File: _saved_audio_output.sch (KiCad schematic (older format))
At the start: 21 parts, among them U8 OPA1664

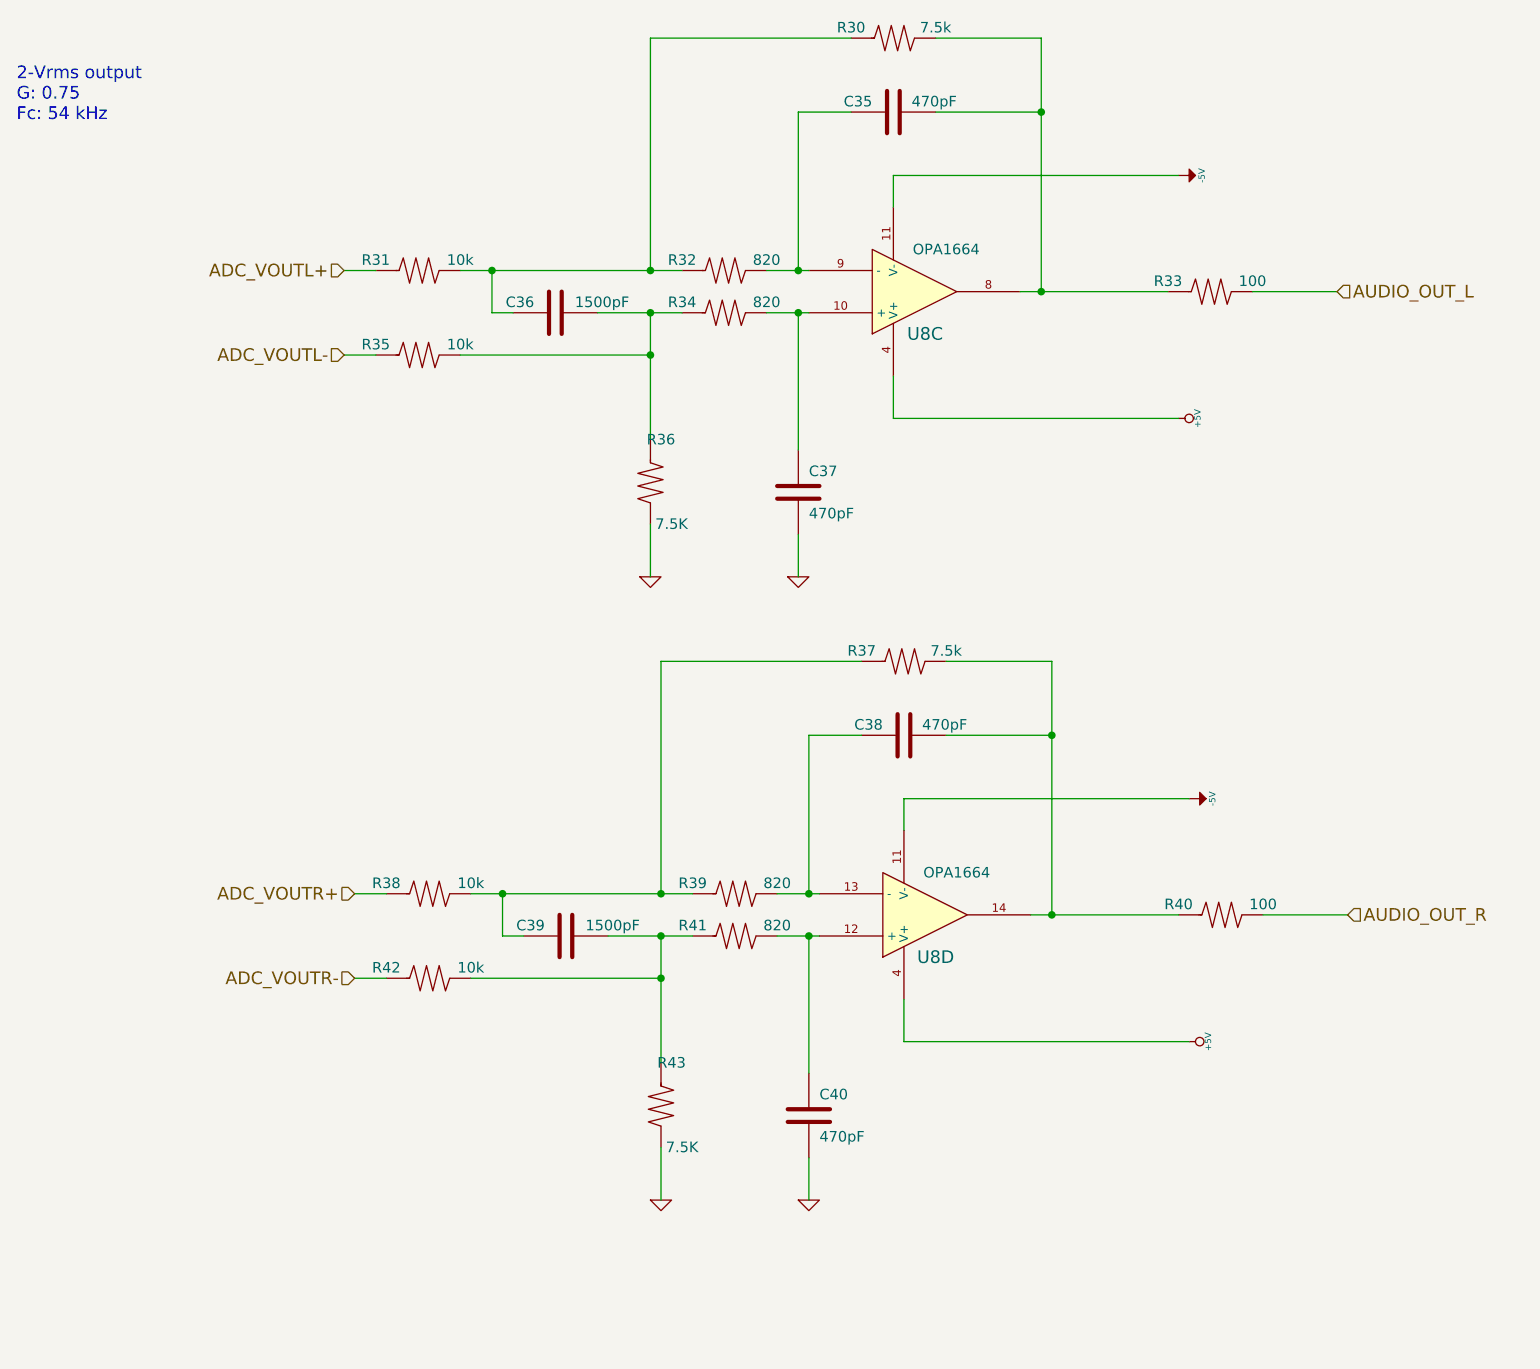
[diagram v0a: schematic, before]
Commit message: Fixed decoupling cap polarity on output op-amp, added bias to analog input, changed capacitor footprints to reflect new capacitor selections
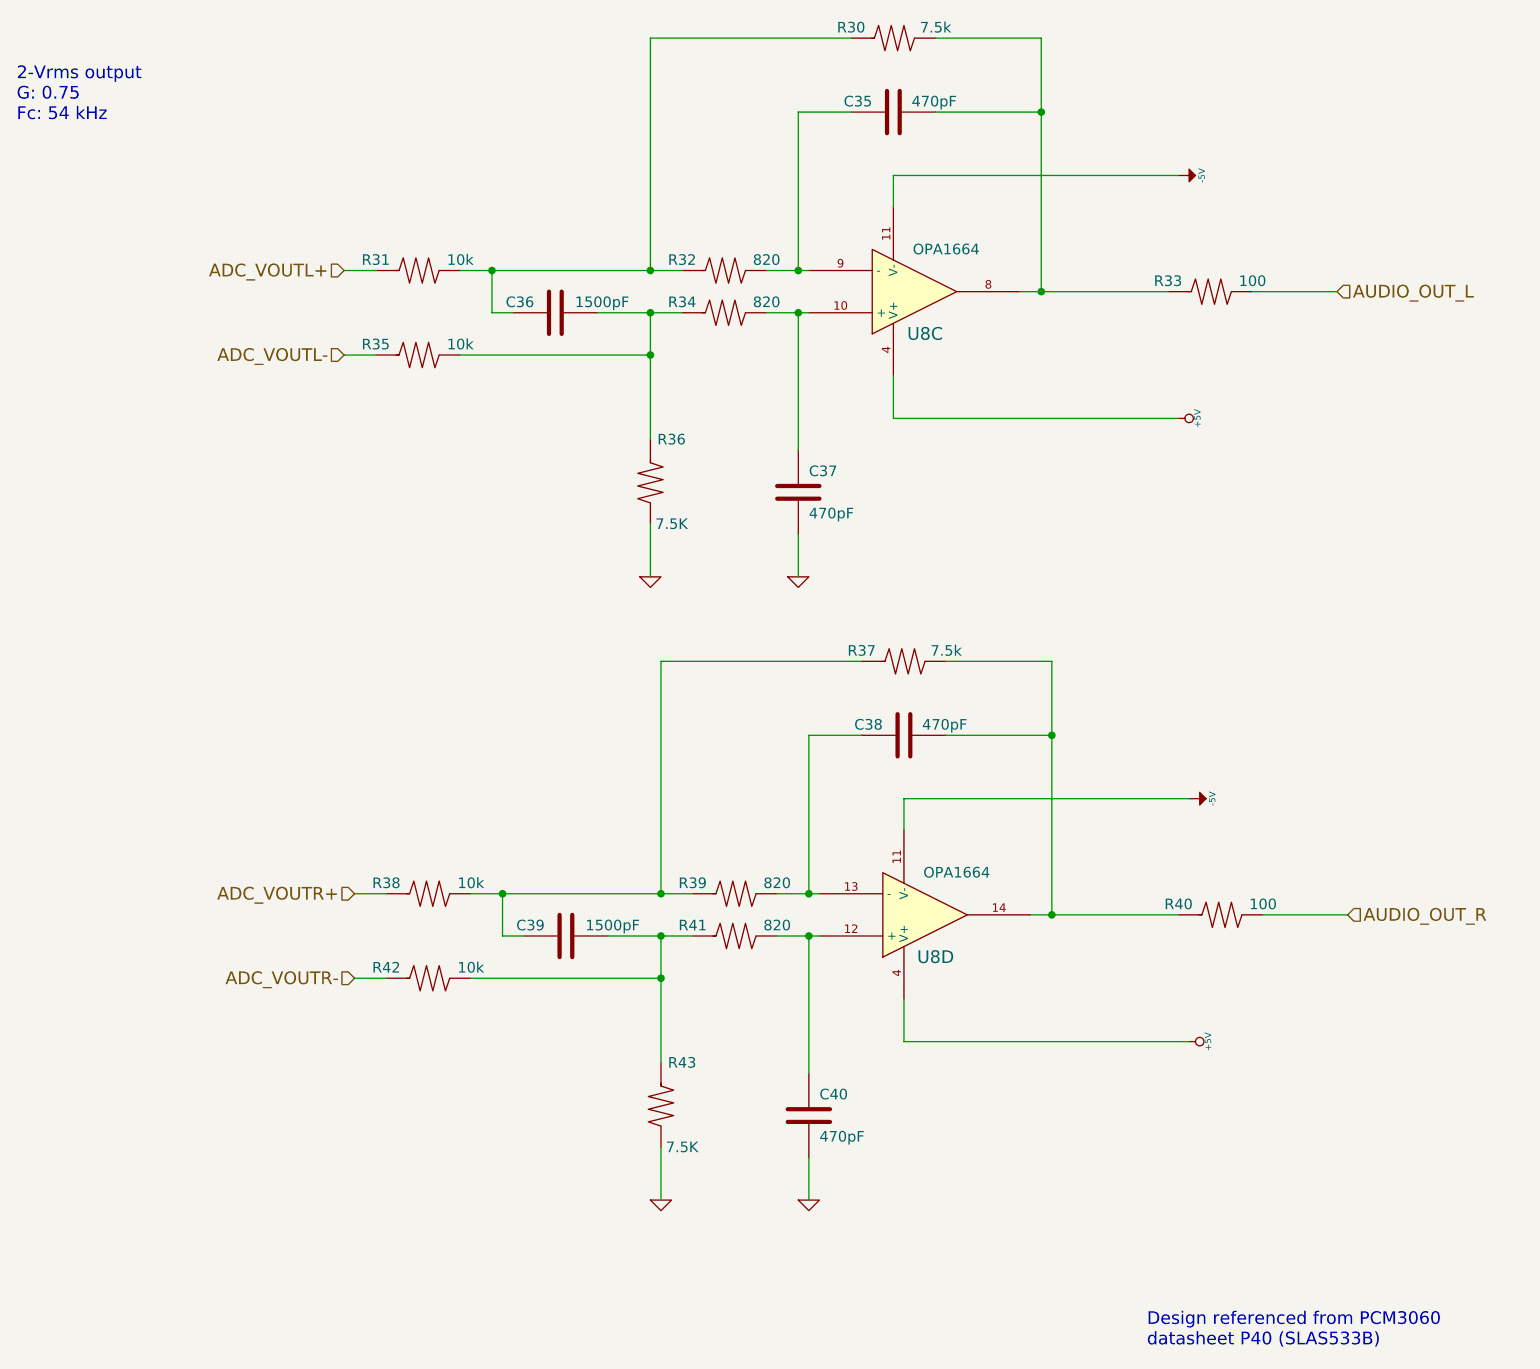
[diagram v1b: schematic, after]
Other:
- note added: "Design referenced from PCM3060\ndatasheet P40 (SLAS533B)"
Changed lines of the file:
@@
 U 1 1 5A4A0B17
 P 4000 2950
-F 0 "R36" V 3800 3000 50  0000 C CNN
+F 0 "R36" V 3800 3050 50  0000 C CNN
 F 1 "7.5K" V 4200 3050 50  0000 C CNN
 F 2 "" H 4000 2950 60  0001 C CNN
@@
 U 1 1 5A4A11F9
 P 4050 5900
-F 0 "R43" V 3850 5950 50  0000 C CNN
+F 0 "R43" V 3850 6000 50  0000 C CNN
 F 1 "7.5K" V 4250 6000 50  0000 C CNN
 F 2 "" H 4050 5900 60  0001 C CNN
@@
 Text Notes 1000 1250 0    60   ~ 0
 2-Vrms output\nG: 0.75\nFc: 54 kHz
+Text Notes 6350 7050 0    60   ~ 0
+Design referenced from PCM3060\ndatasheet P40 (SLAS533B)
 $EndSCHEMATC
